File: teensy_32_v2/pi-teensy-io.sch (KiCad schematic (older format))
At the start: 13 parts

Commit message: more hat
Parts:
- C11: renamed from C?; footprint (none) -> teensy:CPOL-SD-5mm
- D2: renamed from D?; footprint MF_Discrete_Semiconductor_SOD-123 -> MF_Discrete_Semiconductor:MF_Discrete_Semiconductor-SOD-123
- J3, J4, J5, J6: renamed from J?; footprint (none) -> teensy:CJ-2
- R11: renamed from R?; value 390 -> MF-RES-0805-390
- U4: renamed from U?; value PCF8563 -> PCF8563TS/5,118; footprint (none) -> Housings_SSOP:TSSOP-8_3x3mm_Pitch0.65mm
- Y1: renamed from Y?; footprint (none) -> teensy:SC-20S
- gave numbers to parts that had none: 4
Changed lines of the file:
@@
 $EndDescr
 $Comp
-L RESISTOR_0805 R?
+L RESISTOR_0805 R12
 U 1 1 59ED6992
 P 5300 3500
-F 0 "R?" V 5200 3400 45  0000 L BNN
+F 0 "R12" V 5200 3400 45  0000 L BNN
 F 1 "1K" V 5200 3550 45  0000 L BNN
 F 2 "MF_Passives:MF_Passives-R0805" H 5550 3410 20  0001 C CNN
@@
 $EndComp
 $Comp
-L RESISTOR_0805 R?
+L RESISTOR_0805 R13
 U 1 1 59ED6A0D
 P 5300 3850
-F 0 "R?" V 5200 3750 45  0000 L BNN
+F 0 "R13" V 5200 3750 45  0000 L BNN
 F 1 "1K" V 5200 3900 45  0000 L BNN
 F 2 "MF_Passives:MF_Passives-R0805" H 5550 3760 20  0001 C CNN
@@
 $EndComp
 $Comp
-L RESISTOR_0805 R?
+L RESISTOR_0805 R14
 U 1 1 59ED6E9C
 P 6000 2500
-F 0 "R?" V 5900 2400 45  0000 L BNN
+F 0 "R14" V 5900 2400 45  0000 L BNN
 F 1 "2K" V 5900 2550 45  0000 L BNN
 F 2 "MF_Passives:MF_Passives-R0805" H 6250 2410 20  0001 C CNN
@@
 $EndComp
 $Comp
-L RESISTOR_0805 R?
+L RESISTOR_0805 R15
 U 1 1 59ED6EA2
 P 6350 2500
-F 0 "R?" V 6250 2400 45  0000 L BNN
+F 0 "R15" V 6250 2400 45  0000 L BNN
 F 1 "2K" V 6250 2550 45  0000 L BNN
 F 2 "MF_Passives:MF_Passives-R0805" H 6600 2410 20  0001 C CNN
@@
 $EndComp
 $Comp
-L CJ J?
+L CJ J5
 U 1 1 59ED707E
 P 4900 3500
-F 0 "J?" H 4900 3425 39  0000 C CNN
+F 0 "J5" H 4900 3425 39  0000 C CNN
 F 1 "CJ" H 4900 3575 39  0000 C CNN
-F 2 "" H 4900 3500 39  0000 C CNN
+F 2 "teensy:CJ-2" H 4900 3500 39  0001 C CNN
 F 3 "" H 4900 3500 39  0000 C CNN
 	1    4900 3500
@@
 $EndComp
 $Comp
-L CJ J?
+L CJ J6
 U 1 1 59ED70B4
 P 4900 3850
-F 0 "J?" H 4900 3775 39  0000 C CNN
+F 0 "J6" H 4900 3775 39  0000 C CNN
 F 1 "CJ" H 4900 3925 39  0000 C CNN
-F 2 "" H 4900 3850 39  0000 C CNN
+F 2 "teensy:CJ-2" H 4900 3850 39  0001 C CNN
 F 3 "" H 4900 3850 39  0000 C CNN
 	1    4900 3850
@@
 $EndComp
 $Comp
-L CJ J?
+L CJ J3
 U 1 1 59ED70E0
 P 4900 2850
-F 0 "J?" H 4900 2775 39  0000 C CNN
+F 0 "J3" H 4900 2775 39  0000 C CNN
 F 1 "CJ" H 4900 2925 39  0000 C CNN
-F 2 "" H 4900 2850 39  0000 C CNN
+F 2 "teensy:CJ-2" H 4900 2850 39  0001 C CNN
 F 3 "" H 4900 2850 39  0000 C CNN
 	1    4900 2850
@@
 $EndComp
 $Comp
-L CJ J?
+L CJ J4
 U 1 1 59ED7129
 P 4900 3100
-F 0 "J?" H 4900 3025 39  0000 C CNN
+F 0 "J4" H 4900 3025 39  0000 C CNN
 F 1 "CJ" H 4900 3175 39  0000 C CNN
-F 2 "" H 4900 3100 39  0000 C CNN
+F 2 "teensy:CJ-2" H 4900 3100 39  0001 C CNN
 F 3 "" H 4900 3100 39  0000 C CNN
 	1    4900 3100
@@
 $EndComp
 $Comp
-L +3V3 #PWR?
+L +3V3 #PWR020
 U 1 1 59ED724A
 P 6350 950
-F 0 "#PWR?" H 6350 800 50  0001 C CNN
+F 0 "#PWR020" H 6350 800 50  0001 C CNN
 F 1 "+3V3" H 6350 1090 50  0000 C CNN
 F 2 "" H 6350 950 50  0001 C CNN
@@
 T_TX3
 $Comp
-L PCF8563 U?
+L PCF8563 U4
 U 1 1 59ED946C
 P 4650 1850
-F 0 "U?" H 4350 2200 50  0000 L CNN
-F 1 "PCF8563" H 4750 2200 50  0000 L CNN
-F 2 "" H 4650 1850 50  0001 C CNN
+F 0 "U4" H 4350 2200 50  0000 L CNN
+F 1 "PCF8563TS/5,118" H 4750 2200 50  0000 L CNN
+F 2 "Housings_SSOP:TSSOP-8_3x3mm_Pitch0.65mm" H 4650 1850 50  0001 C CNN
 F 3 "" H 4650 1850 50  0001 C CNN
 	1    4650 1850
@@
 $EndComp
 $Comp
-L GND #PWR?
+L GND #PWR021
 U 1 1 59ED9DE4
 P 4650 2450
-F 0 "#PWR?" H 4650 2200 50  0001 C CNN
+F 0 "#PWR021" H 4650 2200 50  0001 C CNN
 F 1 "GND" H 4650 2300 50  0000 C CNN
 F 2 "" H 4650 2450 50  0001 C CNN
@@
 $EndComp
 $Comp
-L Crystal Y?
+L Crystal Y1
 U 1 1 59ED9F2B
 P 4000 1850
-F 0 "Y?" H 4000 2000 50  0000 C CNN
+F 0 "Y1" H 4000 2000 50  0000 C CNN
 F 1 "32 kHz" H 4000 1700 50  0000 C CNN
-F 2 "" H 4000 1850 50  0001 C CNN
+F 2 "teensy:SC-20S" H 4000 1850 50  0001 C CNN
 F 3 "" H 4000 1850 50  0001 C CNN
 	1    4000 1850
@@
 NoConn ~ 5050 2050
 $Comp
-L DIODES_BAT42_SOD-123 D?
+L DIODES_BAT42_SOD-123 D2
 U 1 1 59EDA477
 P 5000 1200
-F 0 "D?" H 5100 1050 45  0000 L BNN
+F 0 "D2" H 5100 1050 45  0000 L BNN
 F 1 "BAT42" H 4850 1050 45  0000 L BNN
-F 2 "MF_Discrete_Semiconductor_SOD-123" H 5188 1279 20  0001 C CNN
+F 2 "MF_Discrete_Semiconductor:MF_Discrete_Semiconductor-SOD-123" H 5188 1279 20  0001 C CNN
 F 3 "" H 5000 1200 60  0001 C CNN
 	1    5000 1200
@@
 	4850 3850 4000 3850
 Wire Wire Line
-	4650 1200 4650 1450
+	4650 950  4650 1450
 Wire Wire Line
 	4650 2250 4650 2450
@@
 	5350 1200 5350 950
 $Comp
-L +5V #PWR?
+L +5V #PWR022
 U 1 1 59EDA676
 P 5350 950
-F 0 "#PWR?" H 5350 800 50  0001 C CNN
+F 0 "#PWR022" H 5350 800 50  0001 C CNN
 F 1 "+5V" H 5350 1090 50  0000 C CNN
 F 2 "" H 5350 950 50  0001 C CNN
@@
 $EndComp
 $Comp
-L CP C?
+L CP C11
 U 1 1 59EDA6A0
 P 3400 2000
-F 0 "C?" H 3425 2100 50  0000 L CNN
+F 0 "C11" H 3425 2100 50  0000 L CNN
 F 1 "0.33F 5.5V" H 3425 1900 50  0000 L CNN
-F 2 "" H 3438 1850 50  0001 C CNN
+F 2 "teensy:CPOL-SD-5mm" H 3438 1850 50  0001 C CNN
 F 3 "" H 3400 2000 50  0001 C CNN
 	1    3400 2000
@@
 $EndComp
 $Comp
-L RESISTOR_0805 R?
+L RESISTOR_0805 R11
 U 1 1 59EDA6D7
 P 3400 1550
-F 0 "R?" V 3300 1450 45  0000 L BNN
-F 1 "390" V 3300 1600 45  0000 L BNN
+F 0 "R11" V 3300 1650 45  0000 L BNN
+F 1 "MF-RES-0805-390" V 3500 1200 45  0000 L BNN
 F 2 "MF_Passives:MF_Passives-R0805" H 3650 1460 20  0001 C CNN
 F 3 "" H 3400 1550 60  0001 C CNN
@@
 	3400 1350 3400 1200
 Connection ~ 4650 1200
+$Comp
+L PWR_FLAG #FLG023
+U 1 1 59F89F7B
+P 4650 950
+F 0 "#FLG023" H 4650 1025 50  0001 C CNN
+F 1 "PWR_FLAG" H 4650 1100 50  0000 C CNN
+F 2 "" H 4650 950 50  0001 C CNN
+F 3 "" H 4650 950 50  0001 C CNN
+	1    4650 950
+	1    0    0    -1
+$EndComp
 $EndSCHEMATC

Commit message: another attempt at Hat layout -- pre routing
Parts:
- removed C11: 0.33F 5.5V, teensy:CPOL-SD-5mm, symbol CP
- removed R11: MF-RES-0805-390, MF_Passives:MF_Passives-R0805, symbol RESISTOR_0805
- added BT1: BC-2009-ND, teensy:BC-2009-ND, symbol Battery_Cell
- added D4: BAT42, MF_Discrete_Semiconductor:MF_Discrete_Semiconductor-SOD-123, symbol DIODES_BAT42_SOD-123
- R12, R13: value 1K -> MF-RES-0603-2K; footprint MF_Passives:MF_Passives-R0805 -> MF_Passives:MF_Passives-R0603
- R14, R15: value 2K -> MF-RES-0603-2K; footprint MF_Passives:MF_Passives-R0805 -> MF_Passives:MF_Passives-R0603
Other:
- moved on the sheet: R12, R13, R14, R15
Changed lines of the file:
@@
 L RESISTOR_0805 R12
 U 1 1 59ED6992
-P 5300 3500
-F 0 "R12" V 5200 3400 45  0000 L BNN
-F 1 "1K" V 5200 3550 45  0000 L BNN
-F 2 "MF_Passives:MF_Passives-R0805" H 5550 3410 20  0001 C CNN
-F 3 "" H 5300 3500 60  0001 C CNN
-	1    5300 3500
+P 5600 3500
+F 0 "R12" V 5500 3400 45  0000 L BNN
+F 1 "MF-RES-0603-2K" V 5500 3550 45  0000 L BNN
+F 2 "MF_Passives:MF_Passives-R0603" H 5850 3410 20  0001 C CNN
+F 3 "" H 5600 3500 60  0001 C CNN
+	1    5600 3500
 	0    1    1    0
 $EndComp
@@
 L RESISTOR_0805 R13
 U 1 1 59ED6A0D
-P 5300 3850
-F 0 "R13" V 5200 3750 45  0000 L BNN
-F 1 "1K" V 5200 3900 45  0000 L BNN
-F 2 "MF_Passives:MF_Passives-R0805" H 5550 3760 20  0001 C CNN
-F 3 "" H 5300 3850 60  0001 C CNN
-	1    5300 3850
+P 5600 3850
+F 0 "R13" V 5500 3750 45  0000 L BNN
+F 1 "MF-RES-0603-2K" V 5500 3900 45  0000 L BNN
+F 2 "MF_Passives:MF_Passives-R0603" H 5850 3760 20  0001 C CNN
+F 3 "" H 5600 3850 60  0001 C CNN
+	1    5600 3850
 	0    1    1    0
 $EndComp
@@
 L RESISTOR_0805 R14
 U 1 1 59ED6E9C
-P 6000 2500
-F 0 "R14" V 5900 2400 45  0000 L BNN
-F 1 "2K" V 5900 2550 45  0000 L BNN
-F 2 "MF_Passives:MF_Passives-R0805" H 6250 2410 20  0001 C CNN
-F 3 "" H 6000 2500 60  0001 C CNN
-	1    6000 2500
+P 6000 2300
+F 0 "R14" V 5900 2200 45  0000 L BNN
+F 1 "MF-RES-0603-2K" V 5900 2350 45  0000 L BNN
+F 2 "MF_Passives:MF_Passives-R0603" H 6250 2210 20  0001 C CNN
+F 3 "" H 6000 2300 60  0001 C CNN
+	1    6000 2300
 	1    0    0    -1
 $EndComp
@@
 L RESISTOR_0805 R15
 U 1 1 59ED6EA2
-P 6350 2500
-F 0 "R15" V 6250 2400 45  0000 L BNN
-F 1 "2K" V 6250 2550 45  0000 L BNN
-F 2 "MF_Passives:MF_Passives-R0805" H 6600 2410 20  0001 C CNN
-F 3 "" H 6350 2500 60  0001 C CNN
-	1    6350 2500
+P 6350 2300
+F 0 "R15" V 6250 2200 45  0000 L BNN
+F 1 "MF-RES-0603-2K" V 6250 2350 45  0000 L BNN
+F 2 "MF_Passives:MF_Passives-R0603" H 6600 2210 20  0001 C CNN
+F 3 "" H 6350 2300 60  0001 C CNN
+	1    6350 2300
 	1    0    0    -1
 $EndComp
@@
 $EndComp
 $Comp
-L +3V3 #PWR020
+L +3V3 #PWR022
 U 1 1 59ED724A
 P 6350 950
-F 0 "#PWR020" H 6350 800 50  0001 C CNN
+F 0 "#PWR022" H 6350 800 50  0001 C CNN
 F 1 "+3V3" H 6350 1090 50  0000 C CNN
 F 2 "" H 6350 950 50  0001 C CNN
@@
 $EndComp
 $Comp
-L GND #PWR021
+L GND #PWR023
 U 1 1 59ED9DE4
 P 4650 2450
-F 0 "#PWR021" H 4650 2200 50  0001 C CNN
+F 0 "#PWR023" H 4650 2200 50  0001 C CNN
 F 1 "GND" H 4650 2300 50  0000 C CNN
 F 2 "" H 4650 2450 50  0001 C CNN
@@
 	4950 3100 7300 3100
 Wire Wire Line
-	6000 2700 6000 2850
+	6000 2500 6000 2850
 Connection ~ 6000 2850
 Wire Wire Line
-	6350 2700 6350 3100
+	6350 2500 6350 3100
 Connection ~ 6350 3100
 Wire Wire Line
-	4950 3500 5100 3500
-Wire Wire Line
-	4950 3850 5100 3850
-Wire Wire Line
-	5500 3500 7300 3500
-Wire Wire Line
-	5500 3850 7300 3850
-Wire Wire Line
-	6350 950  6350 2300
-Wire Wire Line
-	6000 2300 6000 1200
+	4950 3500 5400 3500
+Wire Wire Line
+	4950 3850 5400 3850
+Wire Wire Line
+	5800 3500 7300 3500
+Wire Wire Line
+	5800 3850 7300 3850
+Wire Wire Line
+	6350 950  6350 2100
+Wire Wire Line
+	6000 2100 6000 1200
 Wire Wire Line
 	6000 1200 6350 1200
@@
 	4000 1650 4000 1700
 Wire Wire Line
-	3400 1200 4900 1200
+	4350 1200 4900 1200
 Wire Wire Line
 	5100 1200 5350 1200
@@
 	5350 1200 5350 950
 $Comp
-L +5V #PWR022
+L +5V #PWR024
 U 1 1 59EDA676
 P 5350 950
-F 0 "#PWR022" H 5350 800 50  0001 C CNN
+F 0 "#PWR024" H 5350 800 50  0001 C CNN
 F 1 "+5V" H 5350 1090 50  0000 C CNN
 F 2 "" H 5350 950 50  0001 C CNN
@@
 	1    0    0    -1
 $EndComp
-$Comp
-L CP C11
-U 1 1 59EDA6A0
-P 3400 2000
-F 0 "C11" H 3425 2100 50  0000 L CNN
-F 1 "0.33F 5.5V" H 3425 1900 50  0000 L CNN
-F 2 "teensy:CPOL-SD-5mm" H 3438 1850 50  0001 C CNN
-F 3 "" H 3400 2000 50  0001 C CNN
-	1    3400 2000
-	1    0    0    -1
-$EndComp
-$Comp
-L RESISTOR_0805 R11
-U 1 1 59EDA6D7
-P 3400 1550
-F 0 "R11" V 3300 1650 45  0000 L BNN
-F 1 "MF-RES-0805-390" V 3500 1200 45  0000 L BNN
-F 2 "MF_Passives:MF_Passives-R0805" H 3650 1460 20  0001 C CNN
-F 3 "" H 3400 1550 60  0001 C CNN
-	1    3400 1550
-	-1   0    0    1
-$EndComp
 Wire Wire Line
 	4650 2350 3400 2350
 Wire Wire Line
-	3400 2350 3400 2150
+	3400 2350 3400 1650
 Connection ~ 4650 2350
-Wire Wire Line
-	3400 1850 3400 1750
-Wire Wire Line
-	3400 1350 3400 1200
 Connection ~ 4650 1200
 $Comp
-L PWR_FLAG #FLG023
+L PWR_FLAG #FLG025
 U 1 1 59F89F7B
 P 4650 950
-F 0 "#FLG023" H 4650 1025 50  0001 C CNN
+F 0 "#FLG025" H 4650 1025 50  0001 C CNN
 F 1 "PWR_FLAG" H 4650 1100 50  0000 C CNN
 F 2 "" H 4650 950 50  0001 C CNN
@@
 	1    0    0    -1
 $EndComp
+$Comp
+L DIODES_BAT42_SOD-123 D4
+U 1 1 5A1AF83E
+P 4250 1200
+F 0 "D4" H 4350 1050 45  0000 L BNN
+F 1 "BAT42" H 4100 1050 45  0000 L BNN
+F 2 "MF_Discrete_Semiconductor:MF_Discrete_Semiconductor-SOD-123" H 4438 1279 20  0001 C CNN
+F 3 "" H 4250 1200 60  0001 C CNN
+	1    4250 1200
+	1    0    0    -1
+$EndComp
+Wire Wire Line
+	4150 1200 3400 1200
+Wire Wire Line
+	3400 1200 3400 1350
+$Comp
+L Battery_Cell BT1
+U 1 1 5A1AFB1F
+P 3400 1550
+F 0 "BT1" H 3500 1650 50  0000 L CNN
+F 1 "BC-2009-ND" H 3500 1550 50  0000 L CNN
+F 2 "teensy:BC-2009-ND" V 3400 1610 50  0001 C CNN
+F 3 "" V 3400 1610 50  0001 C CNN
+	1    3400 1550
+	1    0    0    -1
+$EndComp

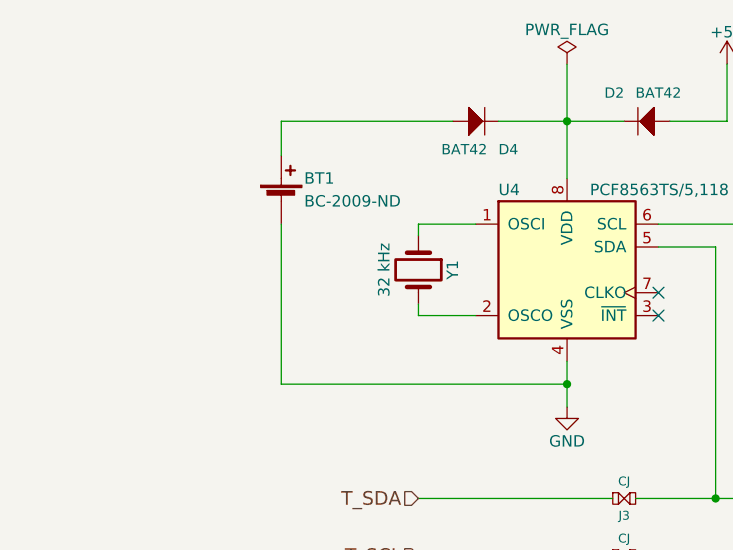
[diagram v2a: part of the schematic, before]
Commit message: Macrofab proto order of teensy hat v2b
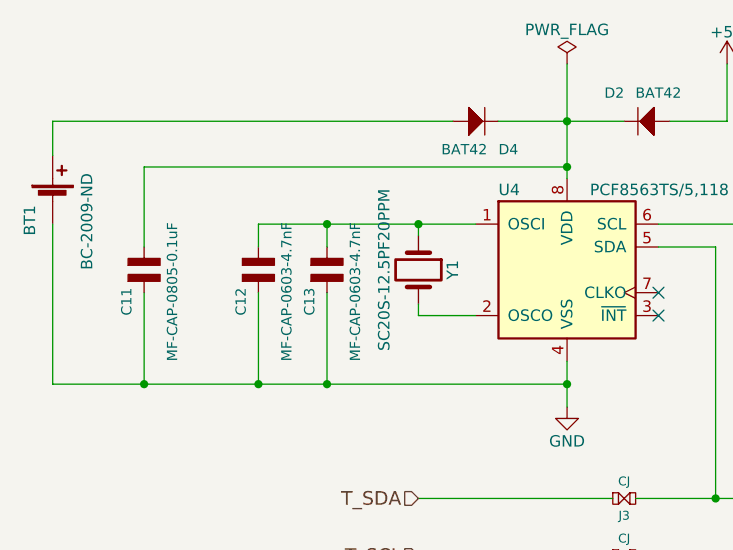
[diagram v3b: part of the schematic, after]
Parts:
- added C11: MF-CAP-0805-0.1uF, MF_Passives:MF_Passives-C0805, symbol CAPACITOR_NP_0805
- added C12, C13: MF-CAP-0603-4.7nF, MF_Passives:MF_Passives-C0603, symbol CAPACITOR_NP_0805
- Y1: value 32 kHz -> SC20S-12.5PF20PPM
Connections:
- net GND: now also C11.2, C12.2, C13.2
- net at U4.1 (OSCI), Y1.1: now also C12.1, C13.1
- net at D2.CATH (CATHODE), D4.CATH (CATHODE), U4.8 (VDD): now also C11.1
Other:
- moved on the sheet: BT1
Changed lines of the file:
@@
 $EndComp
 $Comp
-L +3V3 #PWR022
+L +3V3 #PWR021
 U 1 1 59ED724A
 P 6350 950
-F 0 "#PWR022" H 6350 800 50  0001 C CNN
+F 0 "#PWR021" H 6350 800 50  0001 C CNN
 F 1 "+3V3" H 6350 1090 50  0000 C CNN
 F 2 "" H 6350 950 50  0001 C CNN
@@
 $EndComp
 $Comp
-L GND #PWR023
+L GND #PWR022
 U 1 1 59ED9DE4
 P 4650 2450
-F 0 "#PWR023" H 4650 2200 50  0001 C CNN
+F 0 "#PWR022" H 4650 2200 50  0001 C CNN
 F 1 "GND" H 4650 2300 50  0000 C CNN
 F 2 "" H 4650 2450 50  0001 C CNN
@@
 P 4000 1850
 F 0 "Y1" H 4000 2000 50  0000 C CNN
-F 1 "32 kHz" H 4000 1700 50  0000 C CNN
+F 1 "SC20S-12.5PF20PPM" H 4000 1700 50  0000 C CNN
 F 2 "teensy:SC-20S" H 4000 1850 50  0001 C CNN
 F 3 "" H 4000 1850 50  0001 C CNN
@@
 	-1   0    0    1
 $EndComp
-Wire Wire Line
-	4950 2850 7300 2850
-Wire Wire Line
-	4950 3100 7300 3100
-Wire Wire Line
-	6000 2500 6000 2850
-Connection ~ 6000 2850
-Wire Wire Line
-	6350 2500 6350 3100
-Connection ~ 6350 3100
-Wire Wire Line
-	4950 3500 5400 3500
-Wire Wire Line
-	4950 3850 5400 3850
-Wire Wire Line
-	5800 3500 7300 3500
-Wire Wire Line
-	5800 3850 7300 3850
-Wire Wire Line
-	6350 950  6350 2100
-Wire Wire Line
-	6000 2100 6000 1200
-Wire Wire Line
-	6000 1200 6350 1200
-Connection ~ 6350 1200
-Wire Wire Line
-	4850 2850 4000 2850
-Wire Wire Line
-	4850 3100 4000 3100
-Wire Wire Line
-	4850 3500 4000 3500
-Wire Wire Line
-	4850 3850 4000 3850
-Wire Wire Line
-	4650 950  4650 1450
-Wire Wire Line
-	4650 2250 4650 2450
-Wire Wire Line
-	5050 1650 5550 1650
-Wire Wire Line
-	5550 1650 5550 3100
-Connection ~ 5550 3100
-Wire Wire Line
-	5050 1750 5300 1750
-Wire Wire Line
-	5300 1750 5300 2850
-Connection ~ 5300 2850
-Wire Wire Line
-	4250 2050 4000 2050
-Wire Wire Line
-	4000 2050 4000 2000
-Wire Wire Line
-	4250 1650 4000 1650
-Wire Wire Line
-	4000 1650 4000 1700
-Wire Wire Line
-	4350 1200 4900 1200
-Wire Wire Line
-	5100 1200 5350 1200
-Wire Wire Line
-	5350 1200 5350 950
-$Comp
-L +5V #PWR024
+$Comp
+L +5V #PWR023
 U 1 1 59EDA676
 P 5350 950
-F 0 "#PWR024" H 5350 800 50  0001 C CNN
+F 0 "#PWR023" H 5350 800 50  0001 C CNN
 F 1 "+5V" H 5350 1090 50  0000 C CNN
 F 2 "" H 5350 950 50  0001 C CNN
@@
 	1    0    0    -1
 $EndComp
-Wire Wire Line
-	4650 2350 3400 2350
-Wire Wire Line
-	3400 2350 3400 1650
-Connection ~ 4650 2350
-Connection ~ 4650 1200
-$Comp
-L PWR_FLAG #FLG025
+$Comp
+L PWR_FLAG #FLG024
 U 1 1 59F89F7B
 P 4650 950
-F 0 "#FLG025" H 4650 1025 50  0001 C CNN
+F 0 "#FLG024" H 4650 1025 50  0001 C CNN
 F 1 "PWR_FLAG" H 4650 1100 50  0000 C CNN
 F 2 "" H 4650 950 50  0001 C CNN
@@
 	1    0    0    -1
 $EndComp
-Wire Wire Line
-	4150 1200 3400 1200
-Wire Wire Line
-	3400 1200 3400 1350
 $Comp
 L Battery_Cell BT1
 U 1 1 5A1AFB1F
-P 3400 1550
-F 0 "BT1" H 3500 1650 50  0000 L CNN
-F 1 "BC-2009-ND" H 3500 1550 50  0000 L CNN
-F 2 "teensy:BC-2009-ND" V 3400 1610 50  0001 C CNN
-F 3 "" V 3400 1610 50  0001 C CNN
-	1    3400 1550
-	1    0    0    -1
-$EndComp
+P 2400 1550
+F 0 "BT1" V 2300 1400 50  0000 L CNN
+F 1 "BC-2009-ND" V 2550 1250 50  0000 L CNN
+F 2 "teensy:BC-2009-ND" V 2400 1610 50  0001 C CNN
+F 3 "" V 2400 1610 50  0001 C CNN
+	1    2400 1550
+	1    0    0    -1
+$EndComp
+$Comp
+L CAPACITOR_NP_0805 C?
+U 1 1 5A1C70AC
+P 2800 1850
+AR Path="/59ED6513/5A1C70AC" Ref="C?"  Part="1"
+AR Path="/59ED67C6/5A1C70AC" Ref="C11"  Part="1"
+F 0 "C11" V 2750 1650 45  0000 L BNN
+F 1 "MF-CAP-0805-0.1uF" V 2950 1450 45  0000 L BNN
+F 2 "MF_Passives:MF_Passives-C0805" H 3050 1760 20  0001 C CNN
+F 3 "" H 2800 1850 60  0001 C CNN
+	1    2800 1850
+	1    0    0    -1
+$EndComp
+$Comp
+L CAPACITOR_NP_0805 C?
+U 1 1 5A1C76F9
+P 3600 1850
+AR Path="/59ED6513/5A1C76F9" Ref="C?"  Part="1"
+AR Path="/59ED67C6/5A1C76F9" Ref="C13"  Part="1"
+F 0 "C13" V 3550 1650 45  0000 L BNN
+F 1 "MF-CAP-0603-4.7nF" V 3750 1450 45  0000 L BNN
+F 2 "MF_Passives:MF_Passives-C0603" H 3850 1760 20  0001 C CNN
+F 3 "" H 3600 1850 60  0001 C CNN
+	1    3600 1850
+	1    0    0    -1
+$EndComp
+$Comp
+L CAPACITOR_NP_0805 C?
+U 1 1 5A1C7720
+P 3300 1850
+AR Path="/59ED6513/5A1C7720" Ref="C?"  Part="1"
+AR Path="/59ED67C6/5A1C7720" Ref="C12"  Part="1"
+F 0 "C12" V 3250 1650 45  0000 L BNN
+F 1 "MF-CAP-0603-4.7nF" V 3450 1450 45  0000 L BNN
+F 2 "MF_Passives:MF_Passives-C0603" H 3550 1760 20  0001 C CNN
+F 3 "" H 3300 1850 60  0001 C CNN
+	1    3300 1850
+	1    0    0    -1
+$EndComp
+Wire Wire Line
+	4950 2850 7300 2850
+Wire Wire Line
+	4950 3100 7300 3100
+Wire Wire Line
+	6000 2500 6000 2850
+Connection ~ 6000 2850
+Wire Wire Line
+	6350 2500 6350 3100
+Connection ~ 6350 3100
+Wire Wire Line
+	4950 3500 5400 3500
+Wire Wire Line
+	4950 3850 5400 3850
+Wire Wire Line
+	5800 3500 7300 3500
+Wire Wire Line
+	5800 3850 7300 3850
+Wire Wire Line
+	6350 950  6350 2100
+Wire Wire Line
+	6000 2100 6000 1200
+Wire Wire Line
+	6000 1200 6350 1200
+Connection ~ 6350 1200
+Wire Wire Line
+	4850 2850 4000 2850
+Wire Wire Line
+	4850 3100 4000 3100
+Wire Wire Line
+	4850 3500 4000 3500
+Wire Wire Line
+	4850 3850 4000 3850
+Wire Wire Line
+	4650 950  4650 1450
+Wire Wire Line
+	4650 2250 4650 2450
+Wire Wire Line
+	5050 1650 5550 1650
+Wire Wire Line
+	5550 1650 5550 3100
+Connection ~ 5550 3100
+Wire Wire Line
+	5050 1750 5300 1750
+Wire Wire Line
+	5300 1750 5300 2850
+Connection ~ 5300 2850
+Wire Wire Line
+	4250 2050 4000 2050
+Wire Wire Line
+	4000 2050 4000 2000
+Wire Wire Line
+	3300 1650 4250 1650
+Wire Wire Line
+	4000 1650 4000 1700
+Wire Wire Line
+	4350 1200 4900 1200
+Wire Wire Line
+	5100 1200 5350 1200
+Wire Wire Line
+	5350 1200 5350 950
+Wire Wire Line
+	2400 2350 4650 2350
+Wire Wire Line
+	2400 2350 2400 1650
+Connection ~ 4650 2350
+Connection ~ 4650 1200
+Wire Wire Line
+	4150 1200 2400 1200
+Wire Wire Line
+	2400 1200 2400 1350
+Wire Wire Line
+	2800 1750 2800 1400
+Wire Wire Line
+	2800 1400 4650 1400
+Connection ~ 4650 1400
+Wire Wire Line
+	2800 1950 2800 2350
+Connection ~ 2800 2350
+Wire Wire Line
+	3600 1750 3600 1650
+Connection ~ 4000 1650
+Wire Wire Line
+	3300 1750 3300 1650
+Connection ~ 3600 1650
+Wire Wire Line
+	3600 1950 3600 2350
+Connection ~ 3600 2350
+Wire Wire Line
+	3300 1950 3300 2350
+Connection ~ 3300 2350
 $EndSCHEMATC
